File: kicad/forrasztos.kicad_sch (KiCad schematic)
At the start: 15 parts, among them J1 USART1, J2 DISPLAY_SPI, J3 SWD, SW1 SW_DPDT_x2, U1 STM32F103C8Tx, Y1 32.768kHz

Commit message: work on schematic
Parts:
- removed C5: 100n, symbol Device:C
- added J4: Conn_01x05, symbol Connector_Generic:Conn_01x05
- added R2, R3, R4, R5, R6: R, symbol Device:R
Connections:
- net +3.3V: now also R2.1, R5.1; no longer U1.1 (VBAT)
- net DISP_SPI_MOSI: no longer J2.5 (Pin_5)
- net DISP_SPI_SCK: no longer J2.3 (Pin_3)
- net GND: now also J4.2 (Pin_2), J4.3 (Pin_3)
- net at C8.2, Y1.3: now also R6.1; no longer U1.6 (PD1)
- net at U1.11 (PA1): now also R3.1
- net at U1.12 (PA2): now also R4.1
- net DISP_SPI_MISO: no longer names the net of J2.4 (Pin_4)
- net DISP_SPI_MISO: no longer U1.16 (PA6)
- net DISP_SPI_RST: no longer names the net of U1.14 (PA4)
- net DISP_SPI_RST: no longer J2.2 (Pin_2)
- new net: R6.2, U1.6 (PD1)
- new net DISP_RST: U1.16 (PA6)
- new net NTC: J4.4 (Pin_4), R2.2, R3.2
- new net sensor: J4.5 (Pin_5), R4.2, R5.2
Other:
- moved on the sheet: C1, C2, C3, C4

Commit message: sch kb kesz, meg kell egy kis atdolgozas
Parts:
- removed J1: USART1, symbol Connector_Generic:Conn_01x04
- removed J2: DISPLAY_SPI, symbol Connector_Generic:Conn_01x06
- removed J3: SWD, symbol Connector_Generic:Conn_01x04
- removed J4: Conn_01x05, symbol Connector_Generic:Conn_01x05
- removed SW1: SW_DPDT_x2, Button_Switch_SMD:SW_DPDT_CK_JS202011JCQN, symbol Switch:SW_DPDT_x2
- removed Y1: 32.768kHz, symbol Device:Crystal_GND24
- added C10, C11, C5, C9: 100n, symbol Device:C
- added C12, C13: 1n, symbol Device:C
- added FB1, FB2: FerriteBead, symbol Device:FerriteBead
- added J1: Conn_01x04_Pin, symbol Connector:Conn_01x04_Pin
- added J2: 24V+-, symbol Connector:Conn_01x02_Pin
- added J3: Conn_01x06_Pin, symbol Connector:Conn_01x06_Pin
- added J4: Conn_01x20_Pin, symbol Connector:Conn_01x20_Pin
- added Q1: PMOS, symbol Simulation_SPICE:PMOS
- added Q2: NPN, symbol Simulation_SPICE:NPN
- added R10, R9: R, symbol Device:R
- added R11, R7: 10k, symbol Device:R
- added R12: 1k, symbol Device:R
- added R13, R14, R15, R8: 4k7, symbol Device:R
- added SW1: RotaryEncoder_Switch, symbol Device:RotaryEncoder_Switch
- added U2: 24LC00, symbol Memory_EEPROM:24LC00
- added U3: MCP602, symbol Amplifier_Operational:MCP602
- added U4: ATA00A18S-L, Converter_DCDC:Converter_DCDC_Artesyn_ATA_SMD, symbol Converter_DCDC:ATA00A18S-L
- added U5: AP1117-33, Package_TO_SOT_SMD:SOT-223-3_TabPin2, symbol Regulator_Linear:AP1117-33
- added Y1: 8 MHz, symbol Device:Crystal
- C7, C8: value 22u -> 22pF
- R2: value R -> 2k
- R3: value R -> 1k
- R4: value R -> 470
- R5: value R -> 4k7
- R6: value R -> 10
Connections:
- net +3.3V: now also U1.1 (VBAT), C5.1, FB1.2, J3.1 (Pin_1), J4.2 (Pin_2), R11.2, R7.2, U2.8 (VCC), U5.2 (VO); no longer R2.1, R5.1, U1.9 (VDDA)
- net GND: now also R1.1, R5.2, C10.2, C11.2, C12.2, C13.2, C5.2, C9.2, J1.2 (Pin_2), J2.2 (Pin_2), J3.3 (Pin_3), J4.1 (Pin_1), Q2.3 (E), R9.1, SW1.C, SW1.S1, U2.1 (A0), U2.2 (A1), U2.3 (A2), U2.4 (GND), U2.7 (WP), U4.1 (-VIN), U4.10 (-VOUT), U5.1 (GND)
- net NRST: now also J3.5 (Pin_5), R7.1
- net SWCLK: now also J3.2 (Pin_2)
- net SWDIO: now also J3.4 (Pin_4)
- net sensor: now also U1.11 (PA1), R12.1; no longer R4.2, R5.2
- net at C7.2, U1.5 (PD0): now also Y1.2
- net at C8.2, R6.1: now also Y1.1
- net TEMP: now reaches U1.10 (PA0)
- net TEMP: now also R10.1, U3.1
- net at R3.1: now also R2.2, Q1.2 (G); no longer U1.11 (PA1)
- net at R4.1: now also R5.1, Q2.2 (B); no longer U1.12 (PA2)
- net LCD_RST: now reaches U1.18 (PB0)
- net LCD_RST: now also J4.17 (Pin_17)
- net LCD_CS1: now reaches U1.19 (PB1)
- net LCD_CS2: now reaches U1.20 (PB2)
- net LCD_D2: now reaches U1.21 (PB10)
- net LCD_D2: now also J4.9 (Pin_9)
- net LCD_D3: now reaches U1.22 (PB11)
- net LCD_D3: now also J4.10 (Pin_10)
- net LCD_D4: now reaches U1.25 (PB12)
- net LCD_D4: now also J4.11 (Pin_11)
- net LCD_D5: now reaches U1.26 (PB13)
- net LCD_D5: now also J4.12 (Pin_12)
- net LCD_D6: now reaches U1.27 (PB14)
- net LCD_D6: now also J4.13 (Pin_13)
- net LCD_D7: now reaches U1.28 (PB15)
- net LCD_D7: now also J4.14 (Pin_14)
- net LCD_D0: now reaches U1.29 (PA8)
- net LCD_D0: now also J4.7 (Pin_7)
- net SWO: now reaches U1.39 (PB3)
- net SWO: now also J3.6 (Pin_6)
- net ENC_A: now reaches U1.40 (PB4)
- net ENC_A: now also C12.1, R15.2, SW1.B
- net ENC_B: now reaches U1.41 (PB5)
- net ENC_B: now also C13.1, R14.2, SW1.A
- net i2c_SCL: now reaches U1.42 (PB6)
- net i2c_SCL: now also U2.6 (SCL)
- net i2c_SDA: now reaches U1.43 (PB7)
- net i2c_SDA: now also U2.5 (SDA)
- net ENC_SW: now reaches U1.45 (PB8)
- net ENC_SW: now also R13.2, SW1.S2
- net DISP_RST renamed LCD_RW
- net LCD_RW: now also J4.5 (Pin_5)
- net DISP_SPI_MOSI renamed LCD_RS
- net LCD_RS: now also J4.4 (Pin_4)
- net DISP_SPI_SCK renamed LCD_E
- net LCD_E: now also J4.6 (Pin_6)
- net NTC: no longer names the net of R3.2
- net NTC: now also Q2.1 (C); no longer R2.2
- net USART1_RX: no longer names the net of U1.31 (PA10)
- net USART1_TX renamed LCD_D1
- net LCD_D1: now also J4.8 (Pin_8)
- new net: J1.4 (Pin_4), R11.1, R12.2
- new net: R13.1, R14.1, R15.1
- new net: R10.2, R9.2, U3.2 (-)
- new net: R8.1, U3.3 (+)
- new net: J1.1 (Pin_1), Q1.1 (D), R8.2
- new net +24V: J2.1 (Pin_1), Q1.3 (S), R2.1, U4.16 (+VIN), U4.2 (ON/~{OFF})
- new net +3.3VA: C9.1, FB1.1, U1.9 (VDDA)
- new net +5V: C10.1, FB2.2, U4.9 (+VOUT), U5.3 (VI)
- new net +5VA: C11.1, FB2.1
- new net Earth_Protective: J1.3 (Pin_3)
- new net PWM: R4.2, U1.12 (PA2)
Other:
- moved on the sheet: C1, C2, C3, C4, C6, C7, C8, R1, R6, U1

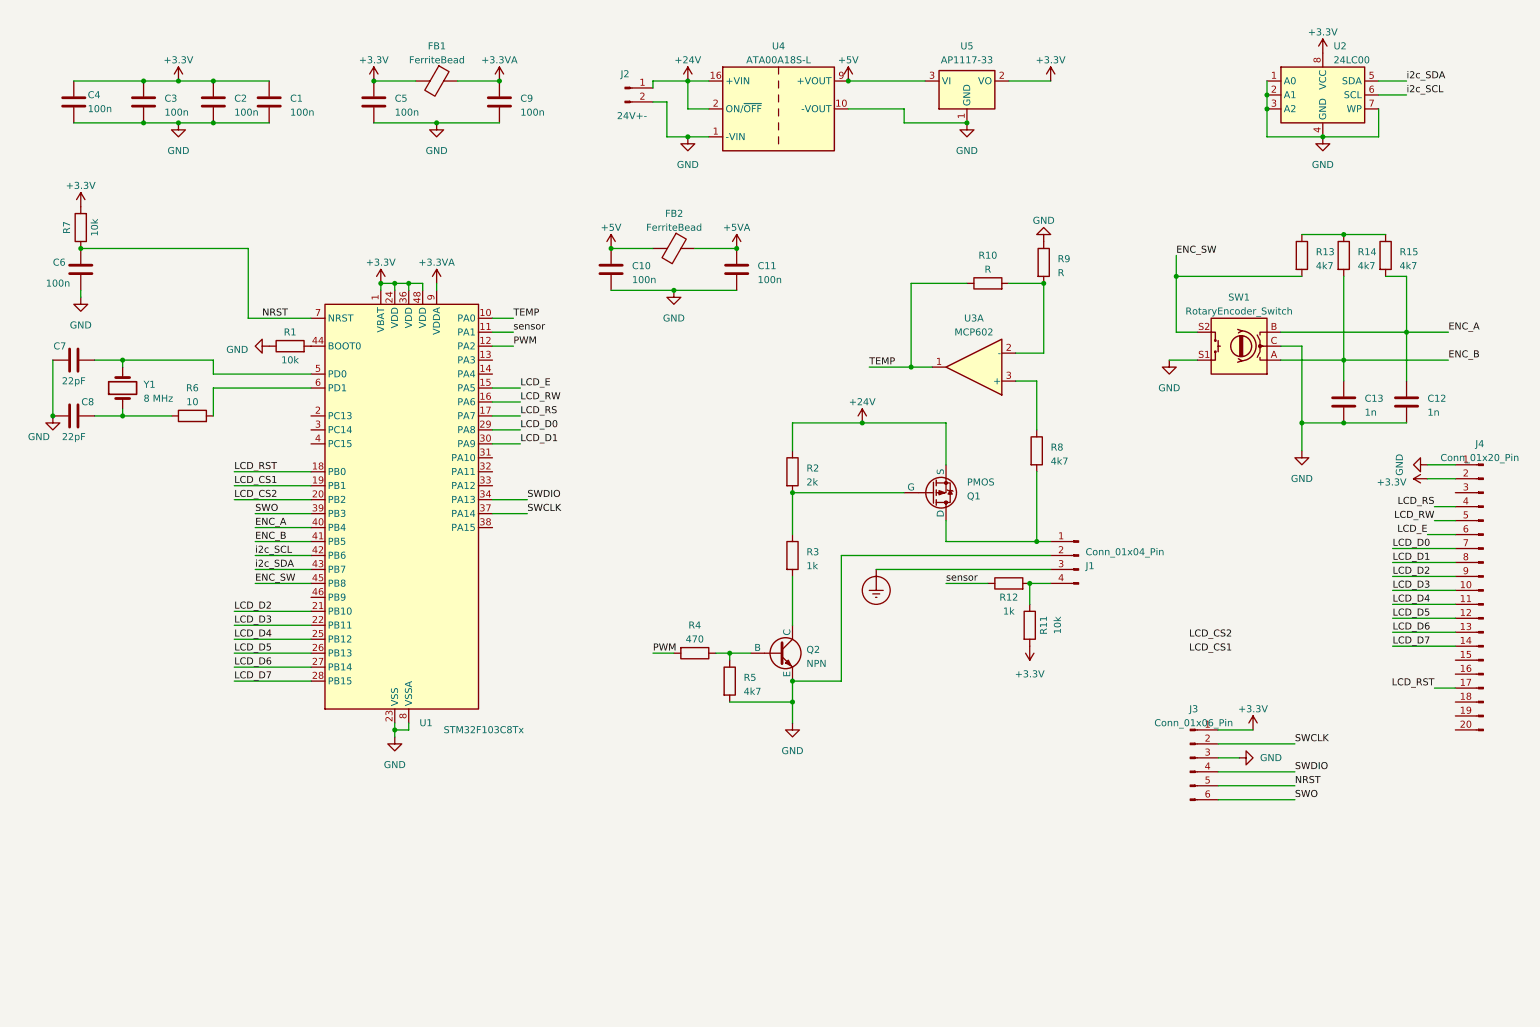
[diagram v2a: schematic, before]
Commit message: added csájníz erősítő
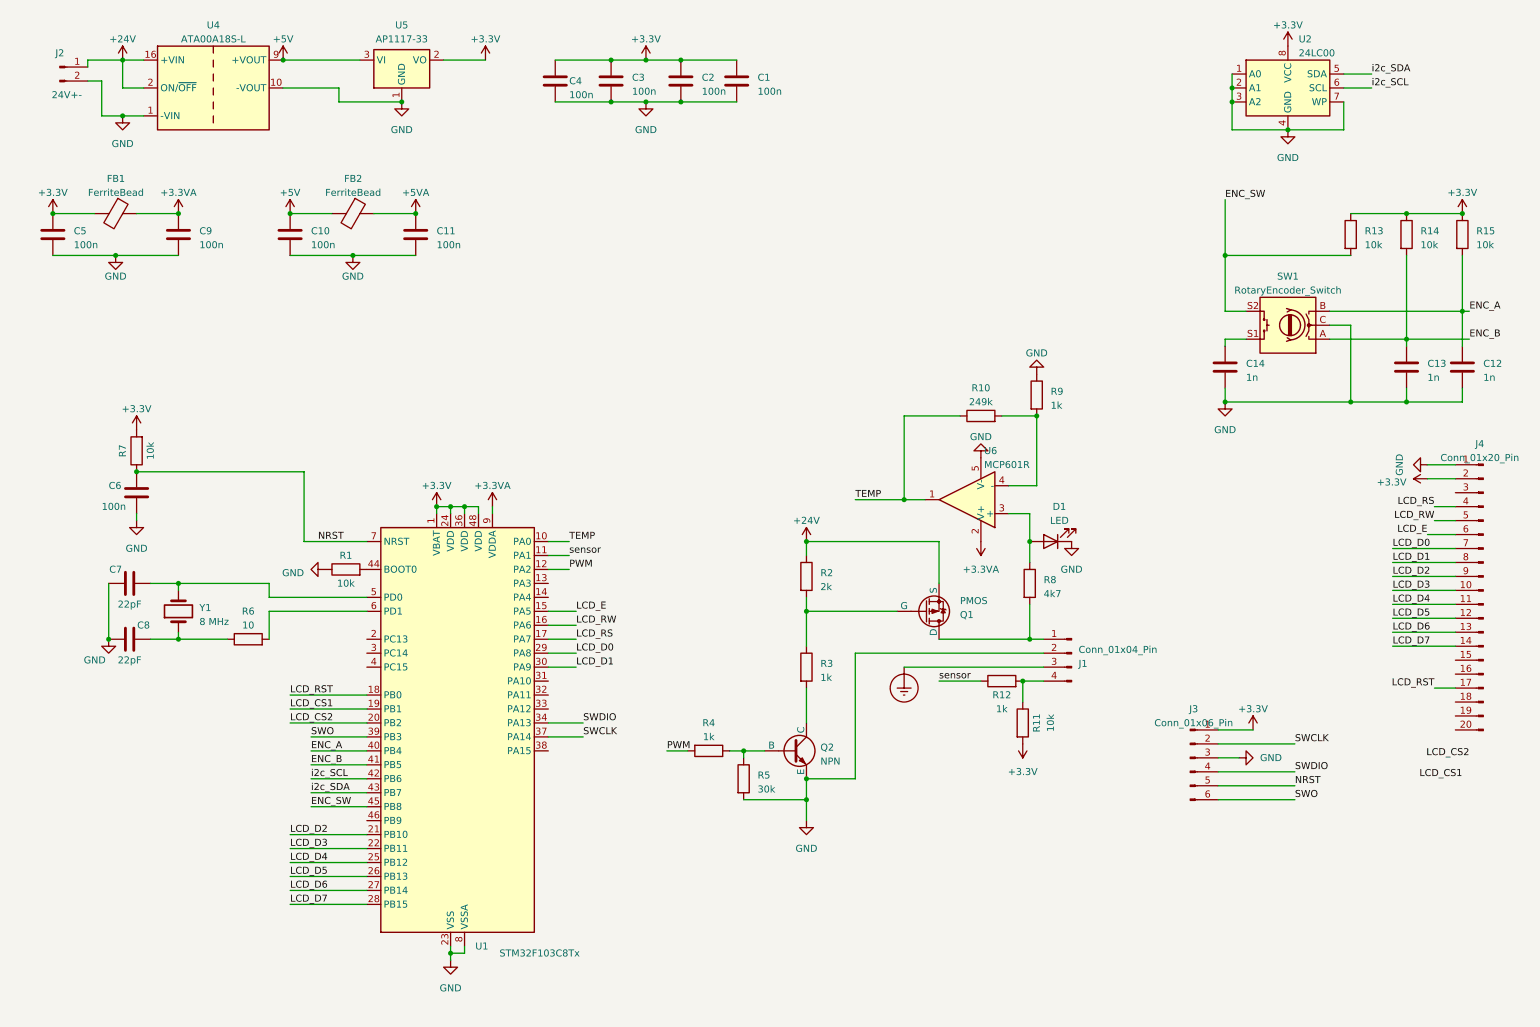
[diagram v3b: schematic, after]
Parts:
- removed U3: MCP602, symbol Amplifier_Operational:MCP602
- added C14: 1n, symbol Device:C
- added D1: LED, symbol Device:LED
- added U6: MCP601R, Package_TO_SOT_SMD:SOT-23-5, symbol Amplifier_Operational:MCP601R
- R10: value R -> 249k
- R13, R14, R15: value 4k7 -> 10k
- R4: value 470 -> 1k
- R5: value 4k7 -> 30k
- R9: value R -> 1k
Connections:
- net +3.3V: now also R13.1, R14.1, R15.1
- net +3.3VA: now also U6.2 (V+)
- net GND: now also C14.2, D1.1 (K), U6.5 (V-); no longer SW1.S1
- net TEMP: now also U6.1
- net at R10.2, R9.2: now also U6.4 (-)
- net at R8.1: now also D1.2 (A), U6.3 (+)
- new net: C14.1, SW1.S1
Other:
- moved on the sheet: C1, C10, C11, C12, C13, C2, C3, C4, C5, C6, C7, C8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

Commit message: replaced analog logic
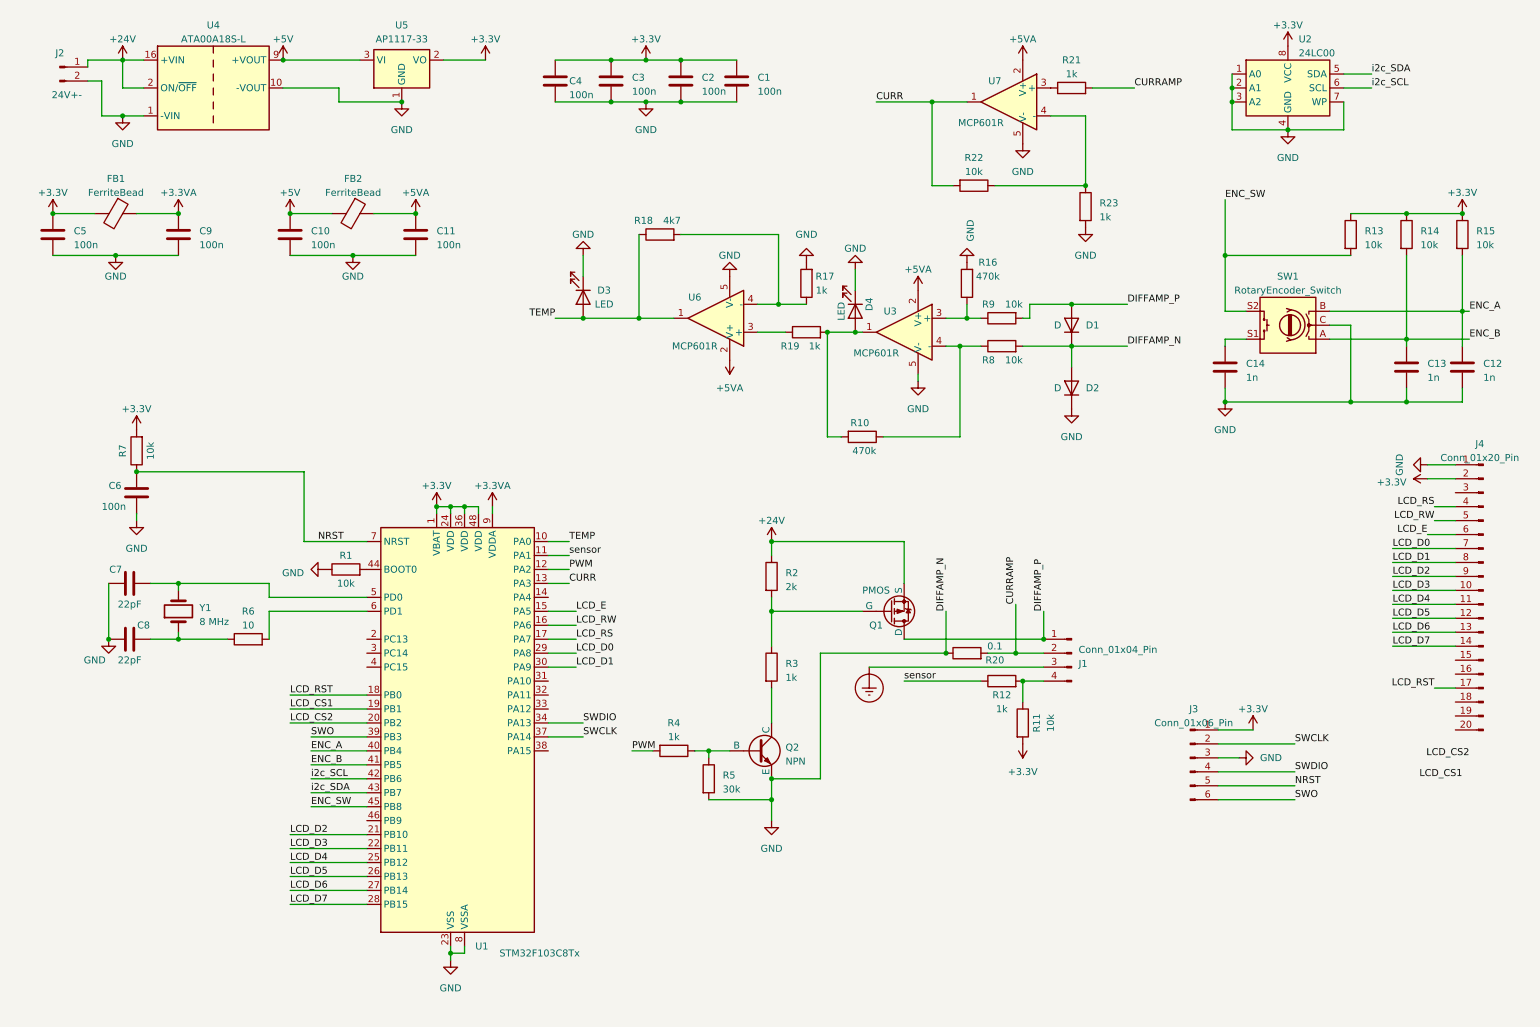
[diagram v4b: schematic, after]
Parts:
- removed D1: LED, symbol Device:LED
- added D1, D2: D, symbol Device:D
- added D3, D4: LED, symbol Device:LED
- added R16: 470k, symbol Device:R
- added R17, R19, R21, R23: 1k, symbol Device:R
- added R18: 4k7, symbol Device:R
- added R20: 0.1, symbol Device:R
- added R22: 10k, symbol Device:R
- added U3, U7: MCP601R, Package_TO_SOT_SMD:SOT-23-5, symbol Amplifier_Operational:MCP601R
- R10: value 249k -> 470k
- R8: value 4k7 -> 10k
- R9: value 1k -> 10k
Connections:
- net +3.3VA: no longer U6.2 (V+)
- net +5VA: now also U6.2 (V+), U3.2 (V+), U7.2 (V+)
- net GND: now also R8.2, D1.1 (K), D2.1 (K), D2.2 (A), D3.1 (K), D4.1 (K), R16.2, R17.2, R20.1, R23.2, U3.5 (V-), U7.5 (V-); no longer J1.2 (Pin_2), R9.1
- net TEMP: now also D3.2 (A), R18.1; no longer R10.1
- net CURR: now reaches U1.13 (PA3)
- net CURR: now also R22.2, U7.1
- net DIFFAMP_P: now reaches J1.1 (Pin_1), Q1.1 (D)
- net DIFFAMP_P: now also R9.2, D1.2 (A); no longer R8.2
- net at R8.1: now also R10.1, U3.4 (-); no longer U6.3 (+)
- new net: R16.1, R9.1, U3.3 (+)
- new net: D4.2 (A), R10.2, R19.2, U3.1
- new net: R21.1, U7.3 (+)
- new net: R17.1, R18.2, U6.4 (-)
- new net: R22.1, R23.1, U7.4 (-)
- new net: R19.1, U6.3 (+)
- new net CURRAMP: J1.2 (Pin_2), R20.2, R21.2
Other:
- moved on the sheet: Q1, Q2, R2, R3, R4, R5
